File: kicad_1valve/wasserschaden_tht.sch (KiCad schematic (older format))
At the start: 18 parts, among them J1 valve out, J2 12V in, J3 sense, U1 stepdown, U2 WeMos_mini, U3 DS18B20

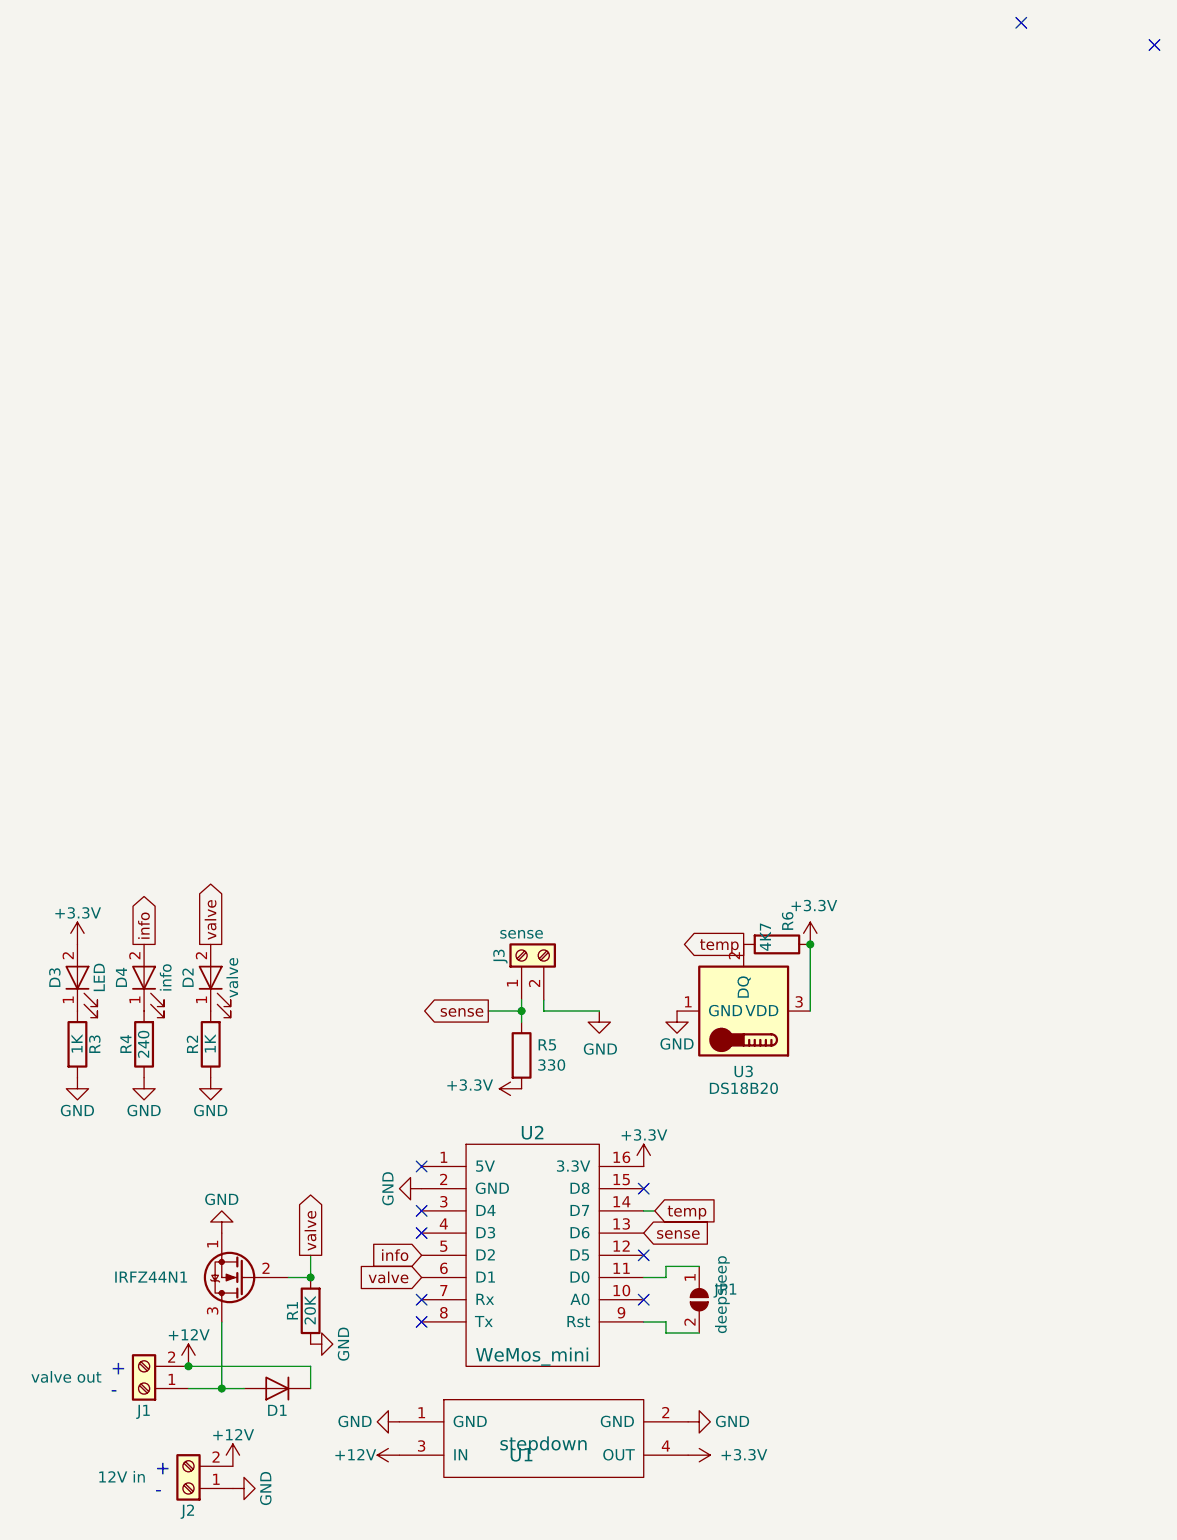
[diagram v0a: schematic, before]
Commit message: make use of net labels more often
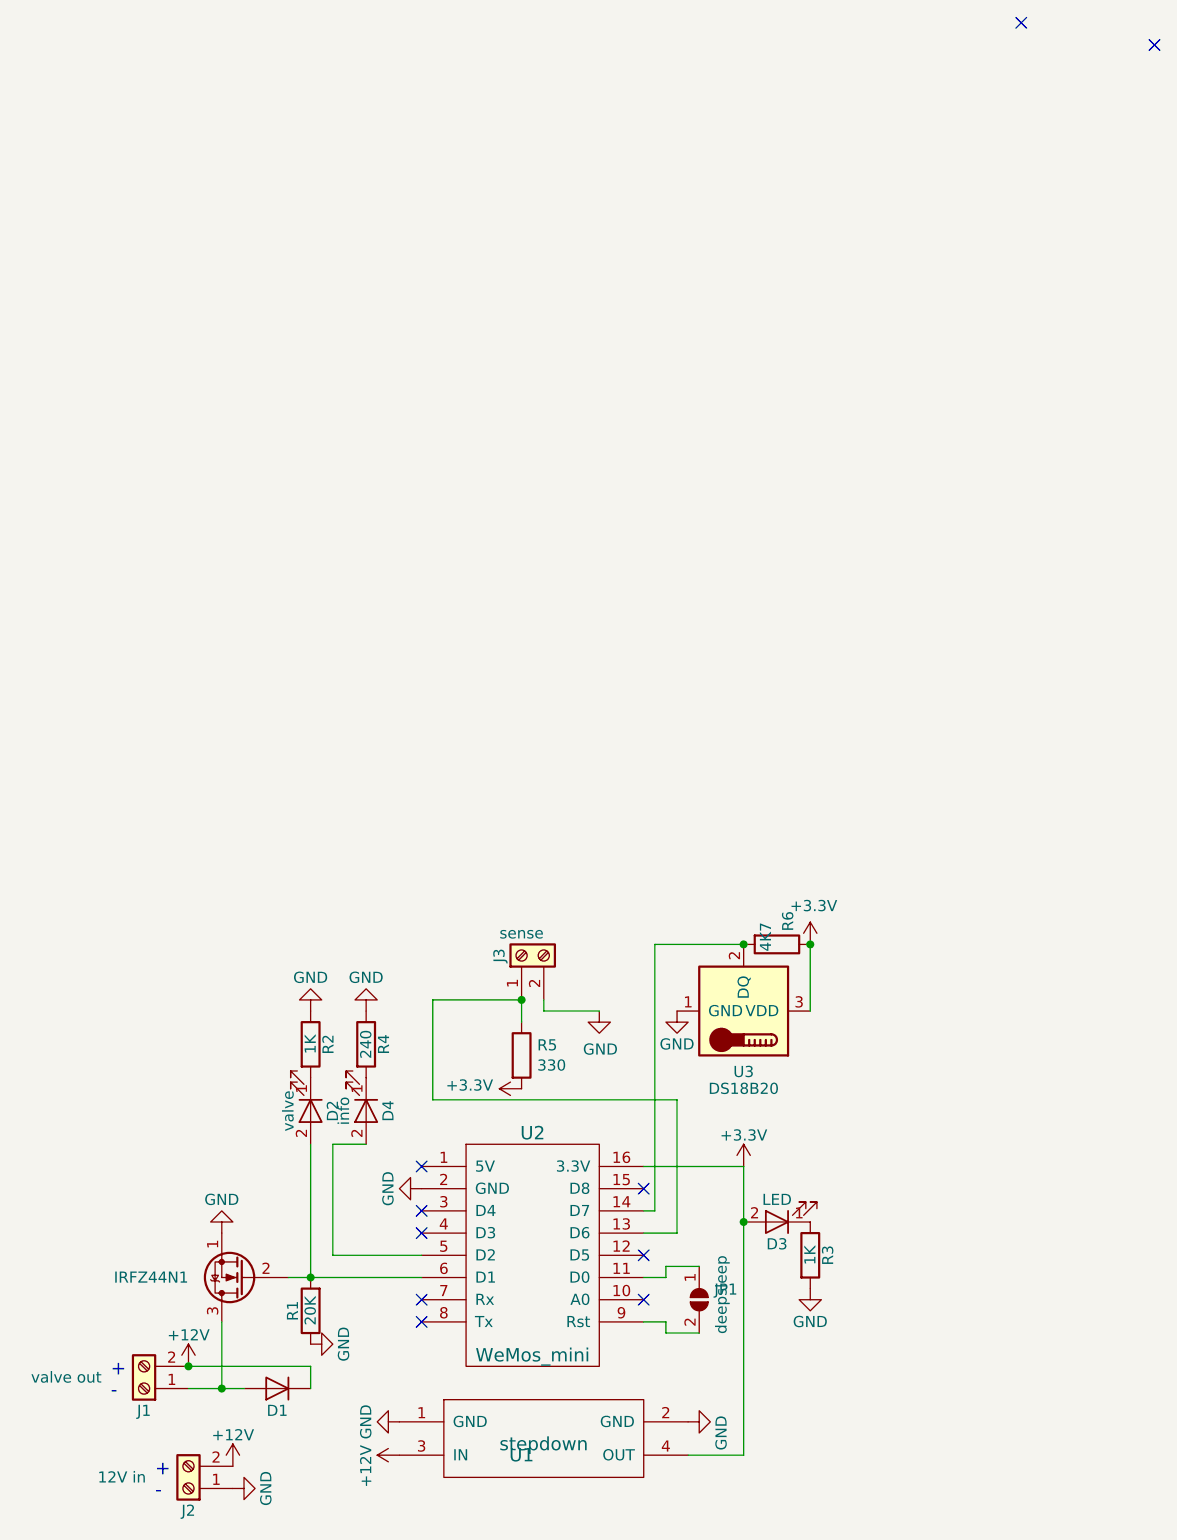
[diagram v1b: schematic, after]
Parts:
- D1: footprint Diodes_SMD:D_SMA_Handsoldering -> Diodes_THT:D_A-405_P7.62mm_Horizontal
- IRFZ44N1: footprint custom:irlz44n_vertical -> custom:irlz44n
- R1, R2, R3, R4, R5, R6: footprint Resistors_SMD:R_0603_HandSoldering -> Resistors_THT:R_Axial_DIN0207_L6.3mm_D2.5mm_P7.62mm_Horizontal
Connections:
- net info: no longer names the net of D4.2 (A), U2.5 (D2)
- net sense: no longer names the net of J3.1 (Pin_1), R5.1, U2.13 (D6)
- net temp: no longer names the net of R6.2, U2.14 (D7), U3.2 (DQ)
- net valve: no longer names the net of D2.2 (A), IRFZ44N1.2 (G), R1.2, U2.6 (D1)
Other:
- moved on the sheet: D2, D3, D4, R2, R3, R4
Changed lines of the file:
@@
 F 0 "IRFZ44N1" H 2950 2250 50  0000 L CNN
 F 1 " " H 2900 2250 50  0000 L CNN
-F 2 "custom:irlz44n_vertical" H 2900 2175 50  0001 L CIN
+F 2 "custom:irlz44n" H 2900 2175 50  0001 L CIN
 F 3 "" H 2700 2250 50  0001 L CNN
 	1    2700 2250
@@
 F 0 "D1" H 2850 2850 50  0000 C CNN
 F 1 " " H 2950 2850 50  0000 C CNN
-F 2 "Diodes_SMD:D_SMA_Handsoldering" H 2850 2750 50  0001 C CNN
+F 2 "Diodes_THT:D_A-405_P7.62mm_Horizontal" H 2850 2750 50  0001 C CNN
 F 3 "" H 2850 2750 50  0001 C CNN
 	1    2850 2750
@@
 	1    0    0    -1
 $EndComp
+Wire Wire Line
+	4500 1750 4950 1750
 $Comp
 L wasserschaden-cache-2018-10-17-20-35-24:GND #PWR04
@@
 P 3400 2900
 F 0 "#PWR04" H 3400 2650 50  0001 C CNN
-F 1 "GND" V 3400 2700 50  0000 C CNN
+F 1 "GND" H 3400 2750 50  0000 C CNN
 F 2 "" H 3400 2900 50  0001 C CNN
 F 3 "" H 3400 2900 50  0001 C CNN
@@
 P 3400 3050
 F 0 "#PWR07" H 3400 2900 50  0001 C CNN
-F 1 "+12V" V 3400 3250 50  0000 C CNN
+F 1 "+12V" H 3350 3200 50  0000 C CNN
 F 2 "" H 3400 3050 50  0001 C CNN
 F 3 "" H 3400 3050 50  0001 C CNN
@@
 F 0 "R1" V 3080 2400 50  0000 C CNN
 F 1 "20K" V 3000 2400 50  0000 C CNN
-F 2 "Resistors_SMD:R_0603_HandSoldering" V 2930 2400 50  0001 C CNN
+F 2 "Resistors_THT:R_Axial_DIN0207_L6.3mm_D2.5mm_P7.62mm_Horizontal" V 2930 2400 50  0001 C CNN
 F 3 "" H 3000 2400 50  0001 C CNN
 	1    3000 2400
@@
 P 4700 2900
 F 0 "#PWR09" H 4700 2650 50  0001 C CNN
-F 1 "GND" V 4700 2700 50  0000 C CNN
+F 1 "GND" H 4650 2750 50  0000 C CNN
 F 2 "" H 4700 2900 50  0001 C CNN
 F 3 "" H 4700 2900 50  0001 C CNN
@@
 	0    -1   -1   0
 $EndComp
+Wire Wire Line
+	4950 3050 4700 3050
 $Comp
 L wasserschaden-cache-2018-10-17-20-35-24:LED D2
 U 1 1 5B2BDC1C
-P 2550 900
-F 0 "D2" H 2550 1000 50  0000 C CNN
-F 1 "valve" H 2550 800 50  0000 C CNN
-F 2 "LEDs:LED_D3.0mm" H 2550 900 50  0001 C CNN
-F 3 "" H 2550 900 50  0001 C CNN
-	1    2550 900
-	0    -1   -1   0
+P 3000 1500
+F 0 "D2" H 3000 1600 50  0000 C CNN
+F 1 "valve" H 3000 1400 50  0000 C CNN
+F 2 "LEDs:LED_D3.0mm" H 3000 1500 50  0001 C CNN
+F 3 "" H 3000 1500 50  0001 C CNN
+	1    3000 1500
+	0    1    1    0
 $EndComp
 $Comp
 L wasserschaden-cache-2018-10-17-20-35-24:R R2
 U 1 1 5B2BDCBD
-P 2550 1200
-F 0 "R2" V 2630 1200 50  0000 C CNN
-F 1 "1K" V 2550 1200 50  0000 C CNN
-F 2 "Resistors_SMD:R_0603_HandSoldering" V 2480 1200 50  0001 C CNN
-F 3 "" H 2550 1200 50  0001 C CNN
-	1    2550 1200
-	-1   0    0    1
+P 3000 1200
+F 0 "R2" V 3080 1200 50  0000 C CNN
+F 1 "1K" V 3000 1200 50  0000 C CNN
+F 2 "Resistors_THT:R_Axial_DIN0207_L6.3mm_D2.5mm_P7.62mm_Horizontal" V 2930 1200 50  0001 C CNN
+F 3 "" H 3000 1200 50  0001 C CNN
+	1    3000 1200
+	1    0    0    -1
 $EndComp
 $Comp
 L wasserschaden-cache-2018-10-17-20-35-24:GND #PWR010
 U 1 1 5B2BDCFD
-P 2550 1350
-F 0 "#PWR010" H 2550 1100 50  0001 C CNN
-F 1 "GND" H 2550 1200 50  0000 C CNN
-F 2 "" H 2550 1350 50  0001 C CNN
-F 3 "" H 2550 1350 50  0001 C CNN
-	1    2550 1350
-	1    0    0    -1
+P 3000 1050
+F 0 "#PWR010" H 3000 800 50  0001 C CNN
+F 1 "GND" H 3000 900 50  0000 C CNN
+F 2 "" H 3000 1050 50  0001 C CNN
+F 3 "" H 3000 1050 50  0001 C CNN
+	1    3000 1050
+	-1   0    0    1
 $EndComp
 Connection ~ 3000 2250
@@
 L wasserschaden-cache-2018-10-17-20-35-24:LED D3
 U 1 1 5B2C19FD
-P 1950 900
-F 0 "D3" H 1950 1000 50  0000 C CNN
-F 1 "LED" H 1950 800 50  0000 C CNN
-F 2 "LEDs:LED_D3.0mm" H 1950 900 50  0001 C CNN
-F 3 "" H 1950 900 50  0001 C CNN
-	1    1950 900
-	0    -1   -1   0
+P 5100 2000
+F 0 "D3" H 5100 2100 50  0000 C CNN
+F 1 "LED" H 5100 1900 50  0000 C CNN
+F 2 "LEDs:LED_D3.0mm" H 5100 2000 50  0001 C CNN
+F 3 "" H 5100 2000 50  0001 C CNN
+	1    5100 2000
+	-1   0    0    1
 $EndComp
 $Comp
 L wasserschaden-cache-2018-10-17-20-35-24:R R3
 U 1 1 5B2C1A03
-P 1950 1200
-F 0 "R3" V 2030 1200 50  0000 C CNN
-F 1 "1K" V 1950 1200 50  0000 C CNN
-F 2 "Resistors_SMD:R_0603_HandSoldering" V 1880 1200 50  0001 C CNN
-F 3 "" H 1950 1200 50  0001 C CNN
-	1    1950 1200
+P 5250 2150
+F 0 "R3" V 5330 2150 50  0000 C CNN
+F 1 "1K" V 5250 2150 50  0000 C CNN
+F 2 "Resistors_THT:R_Axial_DIN0207_L6.3mm_D2.5mm_P7.62mm_Horizontal" V 5180 2150 50  0001 C CNN
+F 3 "" H 5250 2150 50  0001 C CNN
+	1    5250 2150
 	1    0    0    -1
 $EndComp
@@
 L wasserschaden-cache-2018-10-17-20-35-24:GND #PWR011
 U 1 1 5B2C1A09
-P 1950 1350
-F 0 "#PWR011" H 1950 1100 50  0001 C CNN
-F 1 "GND" H 1950 1200 50  0000 C CNN
-F 2 "" H 1950 1350 50  0001 C CNN
-F 3 "" H 1950 1350 50  0001 C CNN
-	1    1950 1350
+P 5250 2300
+F 0 "#PWR011" H 5250 2050 50  0001 C CNN
+F 1 "GND" H 5250 2150 50  0000 C CNN
+F 2 "" H 5250 2300 50  0001 C CNN
+F 3 "" H 5250 2300 50  0001 C CNN
+	1    5250 2300
 	1    0    0    -1
 $EndComp
@@
 L wasserschaden-cache-2018-10-17-20-35-24:LED D4
 U 1 1 5B2C1D4C
-P 2250 900
-F 0 "D4" H 2250 1000 50  0000 C CNN
-F 1 "info" H 2250 800 50  0000 C CNN
-F 2 "LEDs:LED_D3.0mm" H 2250 900 50  0001 C CNN
-F 3 "" H 2250 900 50  0001 C CNN
-	1    2250 900
-	0    -1   -1   0
+P 3250 1500
+F 0 "D4" H 3250 1600 50  0000 C CNN
+F 1 "info" H 3250 1400 50  0000 C CNN
+F 2 "LEDs:LED_D3.0mm" H 3250 1500 50  0001 C CNN
+F 3 "" H 3250 1500 50  0001 C CNN
+	1    3250 1500
+	0    1    1    0
 $EndComp
 $Comp
 L wasserschaden-cache-2018-10-17-20-35-24:R R4
 U 1 1 5B2C1D52
-P 2250 1200
-F 0 "R4" V 2330 1200 50  0000 C CNN
-F 1 "240" V 2250 1200 50  0000 C CNN
-F 2 "Resistors_SMD:R_0603_HandSoldering" V 2180 1200 50  0001 C CNN
-F 3 "" H 2250 1200 50  0001 C CNN
-	1    2250 1200
-	-1   0    0    1
+P 3250 1200
+F 0 "R4" V 3330 1200 50  0000 C CNN
+F 1 "240" V 3250 1200 50  0000 C CNN
+F 2 "Resistors_THT:R_Axial_DIN0207_L6.3mm_D2.5mm_P7.62mm_Horizontal" V 3180 1200 50  0001 C CNN
+F 3 "" H 3250 1200 50  0001 C CNN
+	1    3250 1200
+	1    0    0    -1
 $EndComp
 $Comp
 L wasserschaden-cache-2018-10-17-20-35-24:GND #PWR012
 U 1 1 5B2C1D58
-P 2250 1350
-F 0 "#PWR012" H 2250 1100 50  0001 C CNN
-F 1 "GND" H 2250 1200 50  0000 C CNN
-F 2 "" H 2250 1350 50  0001 C CNN
-F 3 "" H 2250 1350 50  0001 C CNN
-	1    2250 1350
-	1    0    0    -1
-$EndComp
+P 3250 1050
+F 0 "#PWR012" H 3250 800 50  0001 C CNN
+F 1 "GND" H 3250 900 50  0000 C CNN
+F 2 "" H 3250 1050 50  0001 C CNN
+F 3 "" H 3250 1050 50  0001 C CNN
+	1    3250 1050
+	-1   0    0    1
+$EndComp
+Wire Wire Line
+	3250 1650 3100 1650
+Wire Wire Line
+	3100 1650 3100 2150
 $Comp
 L wasserschaden-cache-2018-10-17-20-35-24:+3V3 #PWR013
 U 1 1 5B2C1F93
-P 1950 750
-F 0 "#PWR013" H 1950 600 50  0001 C CNN
-F 1 "+3.3V" H 1950 890 50  0000 C CNN
-F 2 "" H 1950 750 50  0001 C CNN
-F 3 "" H 1950 750 50  0001 C CNN
-	1    1950 750
+P 4950 1750
+F 0 "#PWR013" H 4950 1600 50  0001 C CNN
+F 1 "+3.3V" H 4950 1890 50  0000 C CNN
+F 2 "" H 4950 1750 50  0001 C CNN
+F 3 "" H 4950 1750 50  0001 C CNN
+	1    4950 1750
 	1    0    0    -1
 $EndComp
@@
 NoConn ~ 4500 2150
 Connection ~ 2450 2650
+Wire Wire Line
+	3100 2150 3500 2150
+Wire Wire Line
+	3000 2250 3500 2250
 $Comp
 L wasserschaden-cache-2018-10-17-20-35-24:Screw_Terminal_01x02 J3
@@
 $EndComp
 Wire Wire Line
-	3950 1000 3950 1050
+	3950 1000 3950 1100
 Wire Wire Line
 	4050 1050 4050 1000
@@
 F 0 "R5" H 4020 1296 50  0000 L CNN
 F 1 "330" H 4020 1205 50  0000 L CNN
-F 2 "Resistors_SMD:R_0603_HandSoldering" V 3880 1250 50  0001 C CNN
+F 2 "Resistors_THT:R_Axial_DIN0207_L6.3mm_D2.5mm_P7.62mm_Horizontal" V 3880 1250 50  0001 C CNN
 F 3 "~" H 3950 1250 50  0001 C CNN
 	1    3950 1250
@@
 Connection ~ 2600 2750
 Wire Wire Line
+	3000 1650 3000 2250
+Wire Wire Line
 	3000 2250 2900 2250
+Wire Wire Line
+	4950 1750 4950 2000
+Connection ~ 4950 2000
+Wire Wire Line
+	4950 2000 4950 3050
 $Comp
 L Sensor_Temperature:DS18B20 U3
@@
 F 0 "R6" H 4950 800 50  0000 L CNN
 F 1 "4K7" H 5000 700 50  0000 L CNN
-F 2 "Resistors_SMD:R_0603_HandSoldering" V 5030 750 50  0001 C CNN
+F 2 "Resistors_THT:R_Axial_DIN0207_L6.3mm_D2.5mm_P7.62mm_Horizontal" V 5030 750 50  0001 C CNN
 F 3 "~" H 5100 750 50  0001 C CNN
 	1    5100 750
@@
 Wire Wire Line
 	4500 1950 4550 1950
-$Comp
-L wasserschaden-cache-2018-10-17-20-35-24:+3V3 #PWR?
-U 1 1 5D2E6701
-P 4700 3050
-F 0 "#PWR?" H 4700 2900 50  0001 C CNN
-F 1 "+3.3V" V 4700 3300 50  0000 C CNN
-F 2 "" H 4700 3050 50  0001 C CNN
-F 3 "" H 4700 3050 50  0001 C CNN
-	1    4700 3050
-	0    1    1    0
-$EndComp
-$Comp
-L wasserschaden-cache-2018-10-17-20-35-24:+3V3 #PWR?
-U 1 1 5D2E75DE
-P 4500 1750
-F 0 "#PWR?" H 4500 1600 50  0001 C CNN
-F 1 "+3.3V" H 4500 1890 50  0000 C CNN
-F 2 "" H 4500 1750 50  0001 C CNN
-F 3 "" H 4500 1750 50  0001 C CNN
-	1    4500 1750
-	1    0    0    -1
-$EndComp
-Text GLabel 4550 1950 2    50   Input ~ 0
-temp
-Text GLabel 4950 750  0    50   Output ~ 0
-temp
-Text GLabel 2250 750  1    50   Output ~ 0
-info
-Text GLabel 2550 750  1    50   Output ~ 0
-valve
-Text GLabel 3000 2150 1    50   Output ~ 0
-valve
-Wire Wire Line
-	3000 2150 3000 2250
-Text GLabel 3800 1050 0    50   Output ~ 0
-sense
-Wire Wire Line
-	3800 1050 3950 1050
-Connection ~ 3950 1050
-Wire Wire Line
-	3950 1050 3950 1100
+Wire Wire Line
+	4550 1950 4550 750
+Wire Wire Line
+	4550 750  4950 750
+Connection ~ 4950 750
 NoConn ~ 3500 2050
-Text GLabel 3500 2250 0    50   Input ~ 0
-valve
-Text GLabel 3500 2150 0    50   Input ~ 0
-info
-Text GLabel 4500 2050 2    50   Input ~ 0
-sense
+Wire Wire Line
+	4500 2050 4650 2050
+Wire Wire Line
+	4650 2050 4650 1450
+Wire Wire Line
+	4650 1450 3550 1450
+Wire Wire Line
+	3550 1450 3550 1000
+Wire Wire Line
+	3550 1000 3950 1000
+Connection ~ 3950 1000
 $EndSCHEMATC
